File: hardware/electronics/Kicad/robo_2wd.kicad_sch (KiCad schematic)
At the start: 74 parts, among them J1 Conn_01x06, J10 USB_B, J11 Conn_01x04, J2 Conn_01x06, J3 Conn_01x02, J4 Jack-DC, J5 Conn_01x13, J6 Conn_01x07, J7 Conn_01x04, J8 Conn_01x04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

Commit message: readme in eletronics and some code
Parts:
- D12, D13, D15: value ESD -> Sfi0402-050e560np-lf
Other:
- moved on the sheet: C10, C11, C12, C9, J1, J11, J2, J5, R13, R14, SW1, SW2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

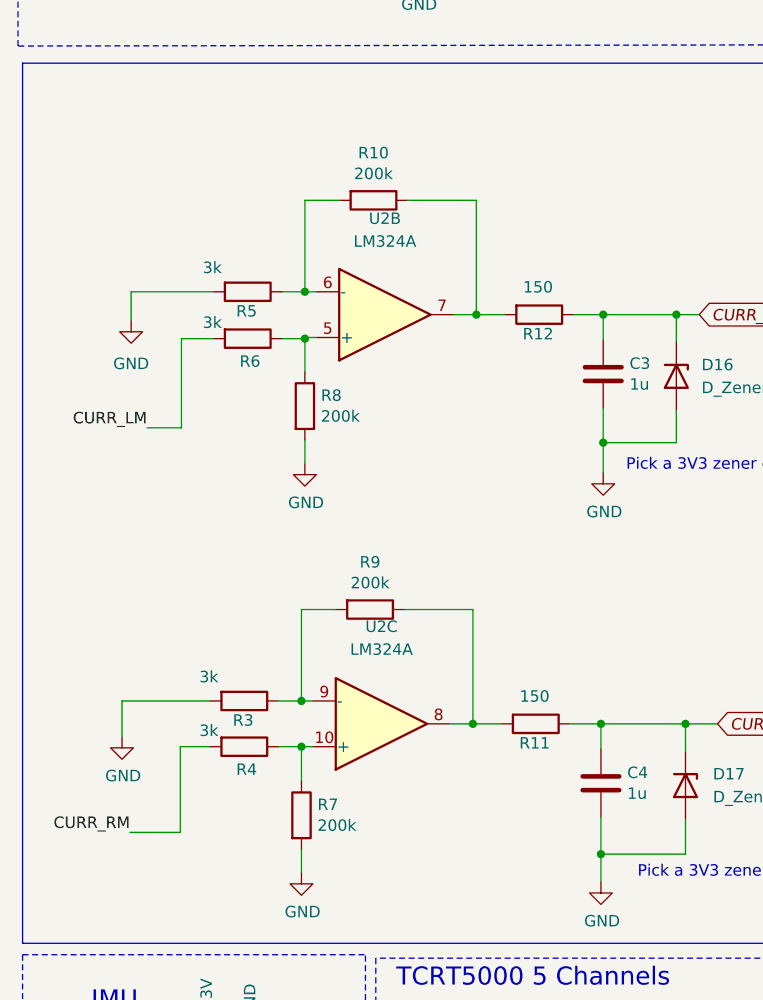
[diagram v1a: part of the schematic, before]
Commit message: update in HW doc
Insertion of current sensor circuit and encoders doc
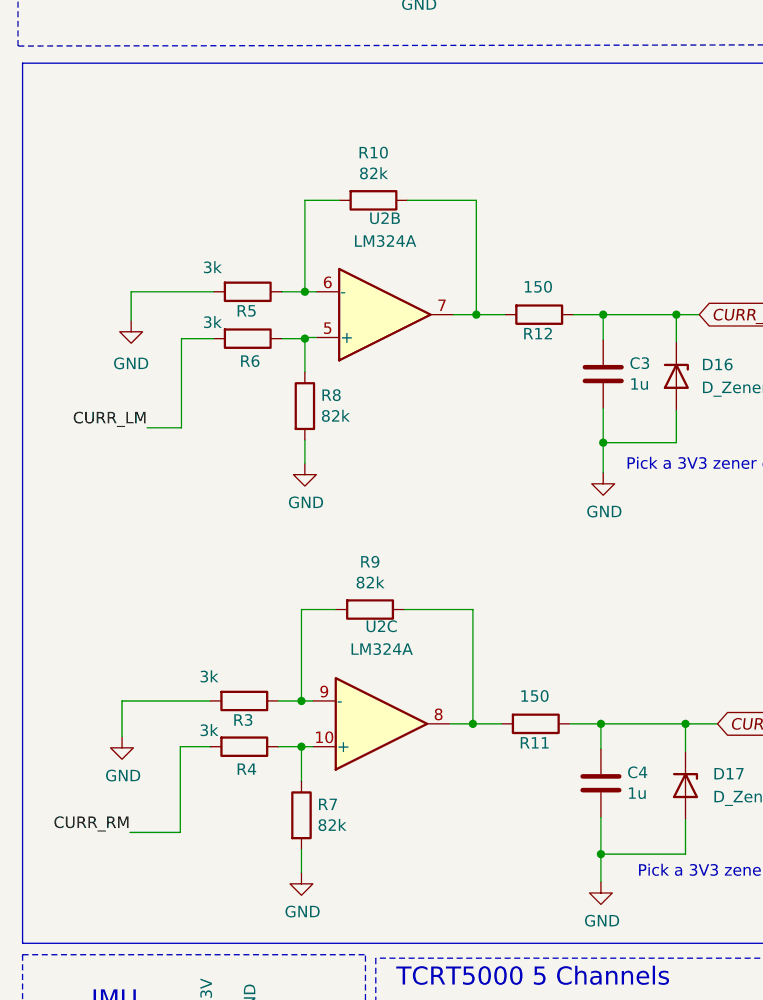
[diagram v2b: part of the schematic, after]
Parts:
- R10, R7, R8, R9: value 200k -> 82k
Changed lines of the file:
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@@
 			)
 		)
-		(property "Value" "200k"
+		(property "Value" "82k"
 			(at 53.721 133.9596 90)
 			(effects
@@
 			)
 		)
-		(property "Value" "200k"
+		(property "Value" "82k"
 			(at 47.879 160.909 0)
 			(effects
@@
 			)
 		)
-		(property "Value" "200k"
+		(property "Value" "82k"
 			(at 47.498 206.375 0)
 			(effects
@@
 			)
 		)
-		(property "Value" "200k"
+		(property "Value" "82k"
 			(at 53.34 179.4256 90)
 			(effects
